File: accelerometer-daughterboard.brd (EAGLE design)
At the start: 17.8 x 25.4 mm, 19 parts, among them U1 LIS3DHTR

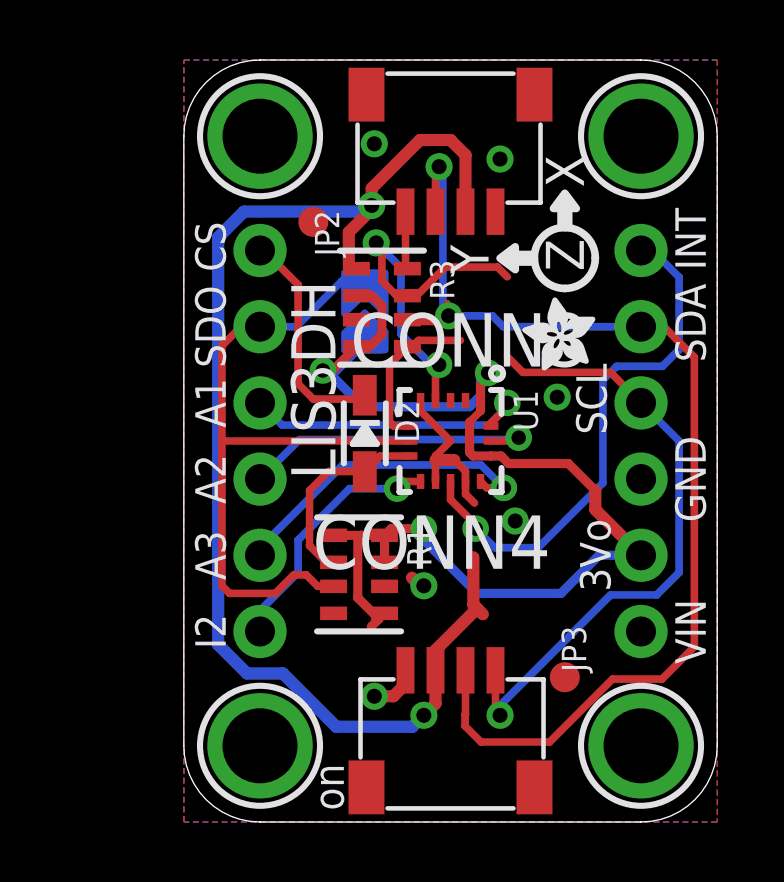
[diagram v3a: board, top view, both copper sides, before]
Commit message: Remove connector headers
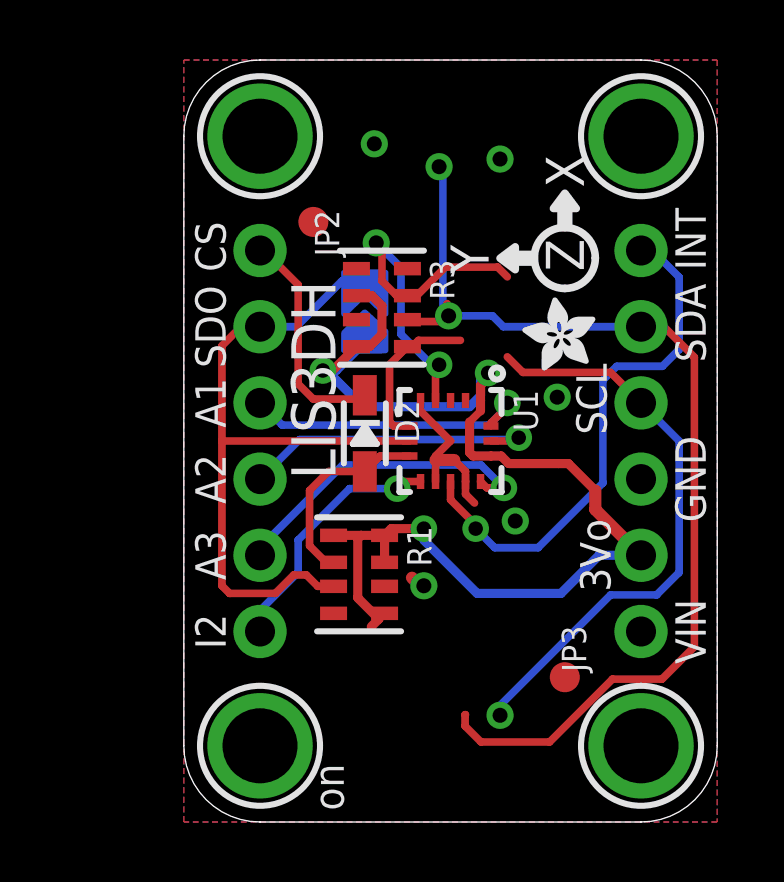
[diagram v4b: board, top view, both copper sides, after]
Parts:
- removed CONN3, CONN4: STEMMA_I2C_QT, microbuilder:JST_SH4
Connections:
- net GND: no longer CONN3.1, CONN4.1
- net SCL: no longer CONN3.4, CONN4.4
- net SDA: no longer CONN3.3, CONN4.3
- net VCC: no longer CONN3.2, CONN4.2
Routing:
- net VCC: track 42.5 -> 0.27 mm, vias 2 -> 0
- net SCL: track 22.8 -> 19.6 mm
- net SDA: track 37.9 -> 35.1 mm
- net GND: track 7.71 -> 6.04 mm, vias 6 -> 5
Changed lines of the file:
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@@
 <attribute name="BOM" value="EXCLUDE" x="2.54" y="22.86" size="1.016" layer="27" font="vector" ratio="14" rot="R90" display="off"/>
-</element>
-<element name="CONN3" library="microbuilder" package="JST_SH4" value="STEMMA_I2C_QT" x="8.89" y="22.86" smashed="yes" rot="R180">
-<attribute name="NAME" x="13.49" y="16.96" size="1.778" layer="25" rot="R180"/>
-</element>
-<element name="CONN4" library="microbuilder" package="JST_SH4" value="STEMMA_I2C_QT" x="8.89" y="2.54" smashed="yes">
-<attribute name="NAME" x="4.29" y="8.44" size="1.778" layer="25"/>
 </element>
 <element name="FID3" library="microbuilder" package="FIDUCIAL_1MM" value="FIDUCIAL_1MM" x="12.7" y="4.826" smashed="yes" rot="R90">
@@
 <signals>
 <signal name="GND" class="1">
-<contactref element="CONN4" pad="1"/>
-<contactref element="CONN3" pad="1"/>
 <polygon width="0.254" layer="1">
 <vertex x="0" y="0"/>
@@
 <vertex x="17.78" y="0"/>
 </polygon>
-<via x="6.35" y="4.191" extent="1-16" drill="0.5"/>
 <via x="10.541" y="22.098" extent="1-16" drill="0.5"/>
-<wire x1="7.39" y1="5.054" x2="7.34" y2="5.004" width="0.4064" layer="1"/>
-<wire x1="7.34" y1="5.004" x2="7.34" y2="4.546" width="0.4064" layer="1"/>
-<wire x1="7.34" y1="4.546" x2="6.985" y2="4.191" width="0.4064" layer="1"/>
-<wire x1="6.985" y1="4.191" x2="6.35" y2="4.191" width="0.4064" layer="1"/>
 <contactref element="U1" pad="5"/>
 <contactref element="U1" pad="10"/>
@@
 <via x="11.049" y="10.033" extent="1-16" drill="0.5"/>
 <via x="12.446" y="14.1605" extent="1-16" drill="0.5"/>
-<wire x1="10.541" y1="22.098" x2="10.39" y2="20.346" width="0" layer="19" extent="1-1"/>
 <wire x1="6.35" y1="22.606" x2="10.541" y2="22.098" width="0" layer="19" extent="1-1"/>
-<wire x1="12.446" y1="14.1605" x2="10.39" y2="20.346" width="0" layer="19" extent="1-1"/>
+<wire x1="12.446" y1="14.1605" x2="10.541" y2="22.098" width="0" layer="19" extent="1-1"/>
 <wire x1="15.24" y1="11.43" x2="12.446" y2="14.1605" width="0" layer="19" extent="1-1"/>
 <wire x1="9.39" y1="11.35" x2="12.446" y2="14.1605" width="0" layer="19" extent="1-1"/>
@@
 <wire x1="7.874" y1="7.874" x2="8.001" y2="7.874" width="0" layer="19" extent="1-1"/>
 <wire x1="6.692" y1="7.855" x2="7.6054" y2="8.1426" width="0" layer="19" extent="1-1"/>
-<wire x1="7.39" y1="5.054" x2="7.874" y2="7.874" width="0" layer="19" extent="1-1"/>
 </signal>
 <signal name="SDA">
-<contactref element="CONN4" pad="3"/>
-<contactref element="CONN3" pad="3"/>
 <wire x1="8.7875" y1="16.872" x2="8.597" y2="16.6815" width="0.254" layer="1"/>
 <wire x1="7.5175" y1="16.6815" x2="8.597" y2="16.6815" width="0.254" layer="1"/>
@@
 <wire x1="8.8265" y1="16.872" x2="8.775" y2="16.9235" width="0.254" layer="1"/>
 <wire x1="8.775" y1="17.283" x2="8.775" y2="16.9235" width="0.254" layer="1"/>
-<wire x1="9.39" y1="5.054" x2="9.39" y2="3.57860625" width="0.254" layer="1"/>
 <wire x1="9.39" y1="3.57860625" x2="9.37539375" y2="3.57860625" width="0.254" layer="1"/>
 <wire x1="9.37539375" y1="3.57860625" x2="9.37539375" y2="3.19760625" width="0.254" layer="1"/>
-<wire x1="8.39" y1="20.346" x2="8.39" y2="21.725" width="0.254" layer="1"/>
 <wire x1="8.39" y1="21.725" x2="8.509" y2="21.844" width="0.254" layer="1"/>
 <via x="8.509" y="21.844" extent="1-16" drill="0.5"/>
@@
 </signal>
 <signal name="SCL">
-<contactref element="CONN4" pad="4"/>
-<contactref element="CONN3" pad="4"/>
-<wire x1="7.39" y1="20.346" x2="7.39" y2="18.509" width="0.254" layer="1"/>
-<wire x1="10.39" y1="5.054" x2="10.39" y2="3.707" width="0.254" layer="1"/>
 <wire x1="10.39" y1="3.707" x2="10.541" y2="3.556" width="0.254" layer="1"/>
 <via x="10.541" y="3.556" extent="1-16" drill="0.5"/>
@@
 <wire x1="15.7607" y1="7.5692" x2="16.51" y2="8.3185" width="0.254" layer="16"/>
 <wire x1="16.51" y1="8.3185" x2="16.51" y2="12.7" width="0.254" layer="16"/>
-<wire x1="10.783" y1="15.506" x2="7.39" y2="18.509" width="0" layer="19" extent="1-1"/>
 </signal>
 <signal name="SCL_3V">
@@
 </signal>
 <signal name="VCC" class="1">
-<contactref element="CONN3" pad="2"/>
-<contactref element="CONN4" pad="2"/>
-<wire x1="9.652" y1="8.824" x2="9.652" y2="7.239" width="0.4064" layer="1"/>
-<wire x1="9.652" y1="7.239" x2="9.7765" y2="7.1145" width="0.4064" layer="1"/>
-<wire x1="9.7765" y1="7.1145" x2="9.967" y2="6.924" width="0.4064" layer="1"/>
-<wire x1="8.39" y1="5.054" x2="8.39" y2="5.728" width="0.4064" layer="1"/>
-<wire x1="8.39" y1="5.728" x2="9.7765" y2="7.1145" width="0.4064" layer="1"/>
-<wire x1="9.39" y1="20.346" x2="9.39" y2="22.233" width="0.4064" layer="1"/>
-<wire x1="9.39" y1="22.233" x2="8.89" y2="22.733" width="0.4064" layer="1"/>
-<wire x1="8.89" y1="22.733" x2="7.874" y2="22.733" width="0.4064" layer="1"/>
-<wire x1="6.262" y1="20.5495" x2="6.262" y2="21.121" width="0.4064" layer="1"/>
-<wire x1="7.874" y1="22.733" x2="6.262" y2="21.121" width="0.4064" layer="1"/>
-<via x="6.262" y="20.5495" extent="1-16" drill="0.5"/>
-<wire x1="6.262" y1="20.5495" x2="6.262" y2="20.4225" width="0.4064" layer="1"/>
-<wire x1="6.262" y1="20.4225" x2="5.5" y2="19.6605" width="0.4064" layer="1"/>
-<wire x1="5.5" y1="19.6605" x2="5.5" y2="18.699" width="0.4064" layer="1"/>
-<wire x1="2.003425" y1="20.3454" x2="6.0579" y2="20.3454" width="0.4064" layer="16"/>
-<wire x1="6.262" y1="20.5495" x2="6.0579" y2="20.3454" width="0.4064" layer="16"/>
-<via x="8.001" y="3.556" extent="1-16" drill="0.5"/>
-<wire x1="8.39" y1="5.054" x2="8.39" y2="3.945" width="0.4064" layer="1"/>
-<wire x1="8.39" y1="3.945" x2="8.001" y2="3.556" width="0.4064" layer="1"/>
 <contactref element="JP3" pad="1"/>
 <wire x1="15.047" y1="6.543" x2="15.24" y2="6.35" width="0.4064" layer="1"/>
-<wire x1="8.001" y1="3.556" x2="7.62" y2="3.175" width="0.4064" layer="16"/>
-<wire x1="2.105025" y1="4.953" x2="1.143" y2="5.915025" width="0.4064" layer="16"/>
-<wire x1="1.143" y1="19.484975" x2="2.003425" y2="20.3454" width="0.4064" layer="16"/>
-<wire x1="7.62" y1="3.175" x2="5.08" y2="3.175" width="0.4064" layer="16"/>
-<wire x1="5.08" y1="3.175" x2="3.302" y2="4.953" width="0.4064" layer="16"/>
-<wire x1="3.302" y1="4.953" x2="2.105025" y2="4.953" width="0.4064" layer="16"/>
-<wire x1="1.143" y1="5.915025" x2="1.143" y2="19.484975" width="0.4064" layer="16"/>
-<wire x1="9.967" y1="6.924" x2="15.047" y2="6.543" width="0" layer="19" extent="1-1"/>
 </signal>
 <signal name="CS">

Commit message: Remove through-holes
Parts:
- removed JP2, JP3: (no value), microbuilder:1X06_ROUND_70
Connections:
- removed net SCL: JP3.4
- removed net SDA: JP3.5
- removed net VCC: JP3.1
- net 3.3V: no longer JP3.2
- net ADC1: no longer JP2.3
- net ADC2: no longer JP2.4
- net ADC3: no longer JP2.5
- net CS: no longer JP2.1
- net GND: no longer JP3.3
- net INT1: no longer JP3.6
- net INT2: no longer JP2.6
- net SDO: no longer JP2.2
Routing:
- net SDA: track 35.1 -> 0.00 mm, vias 2 -> 0
- net SCL: track 19.6 -> 0.00 mm, vias 1 -> 0
- net 3.3V: track 40.1 -> 36.5 mm
- net ADC2: track 10.2 -> 8.30 mm
- net SDO: track 24.2 -> 22.3 mm
- net ADC1: track 9.92 -> 8.88 mm
- net INT2: track 8.46 -> 7.76 mm

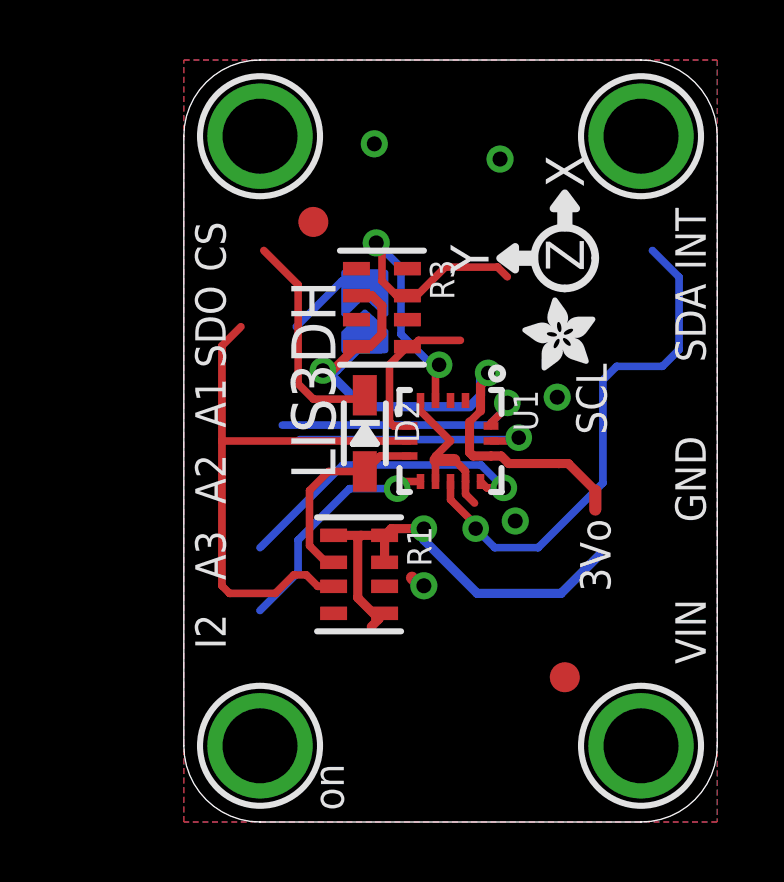
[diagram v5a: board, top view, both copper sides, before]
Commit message: Hardwire CS to I2C mode; add pads; remove un-used board elements
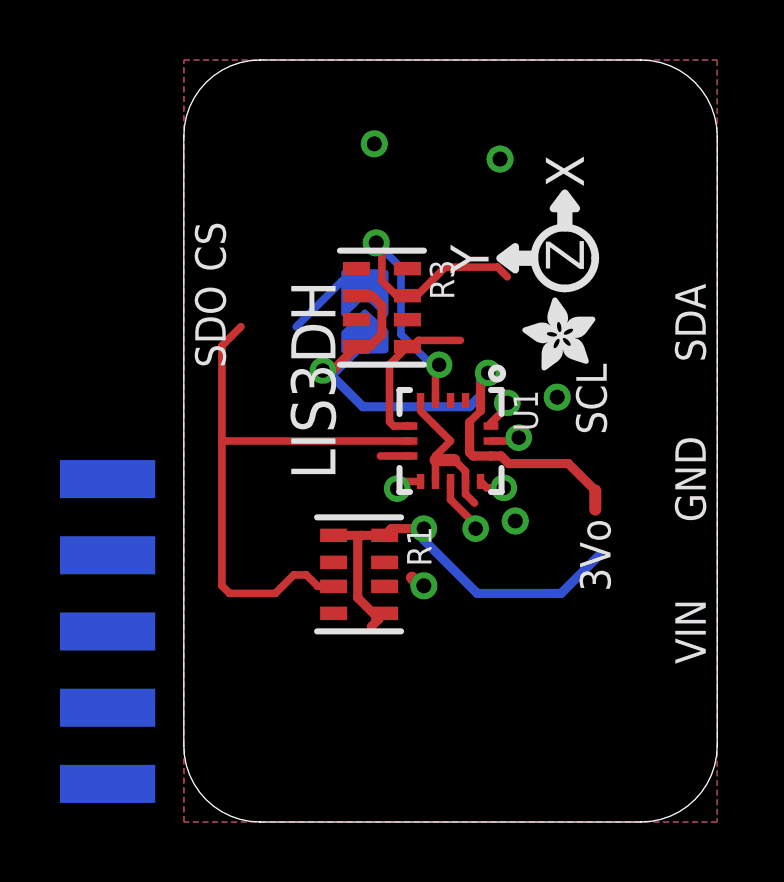
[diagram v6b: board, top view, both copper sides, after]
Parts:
- removed D2: 1N4148, microbuilder:SOD-323
- removed FID3, FID4: FIDUCIAL_1MM, microbuilder:FIDUCIAL_1MM
- removed U$17, U$19, U$21: MOUNTINGHOLE2.5, microbuilder:MOUNTINGHOLE_2.5_PLATED
- removed U$30, U$31: (no value), silks:STEMMAQT
- U$1: value MOUNTINGHOLE2.5 -> ALEX_CONN5; device microbuilder:MOUNTINGHOLE_2.5_PLATED -> TestBoard_2_2_LiPo:ALEX_CONN5
- moved U$1 6.35 mm to (-2.54, 6.35), flipped to the bottom, turned to 0 degrees
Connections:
- removed net CS: D2.C
- removed net N$2: D2.A, R1.2, U1.8
- net 3.3V: now also U1.8; no longer R1.7
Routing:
- net INT1: track 17.4 -> 1.92 mm
- net ADC3: track 10.5 -> 0.87 mm
- net CS: track 7.40 -> 0.00 mm
- net ADC2: track 8.30 -> 1.06 mm
- net ADC1: track 8.88 -> 1.99 mm
- net INT2: track 7.76 -> 0.88 mm
- net N$2: track 6.70 -> 0.00 mm
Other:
- board text removed: "A1"
- board text removed: "A2"
- board text removed: "A3"
- board text removed: "I2"
- board text removed: "INT"
- board text removed: "VLogic/Vcc: 3-5VDC"
- board text removed: "on"

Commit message: USe 0603 resistors
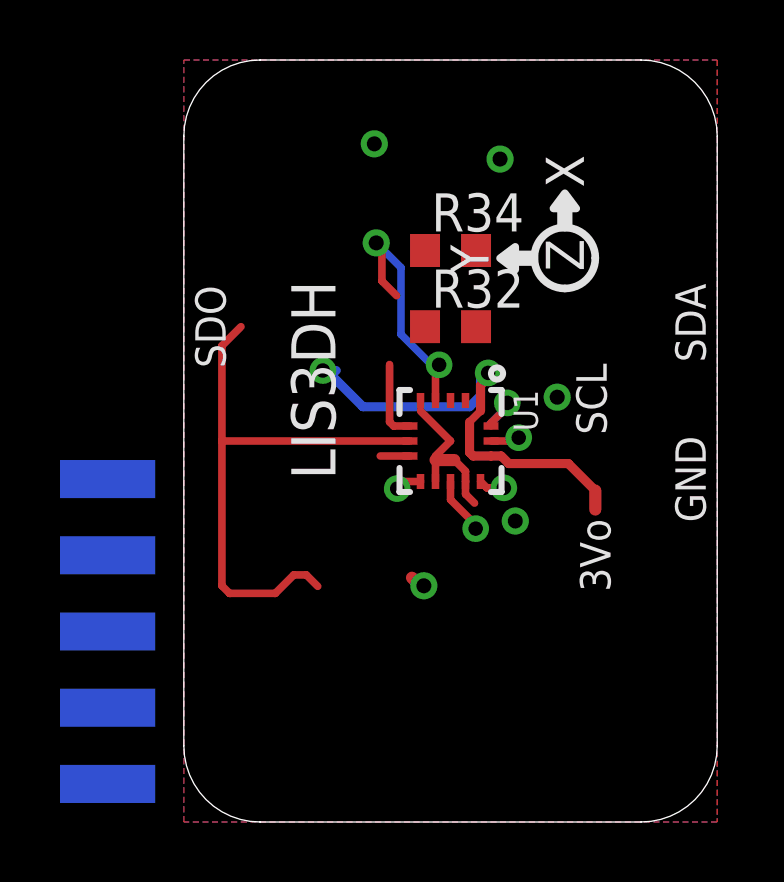
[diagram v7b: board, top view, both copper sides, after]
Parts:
- removed R1, R3: 10K, microbuilder:RESPACK_4X0603
- removed SJ1: (no value), microbuilder:SOLDERJUMPER_ARROW_NOPASTE
- removed U$12: (no value), microbuilder:ADAFRUIT_2.5MM
- added R32, R34: 10K, rcl:R0603
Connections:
- net 3.3V: now also R32.2, R34.2; no longer R1.1, R1.8, R3.2, R3.4, SJ1.1
- net GND: no longer R1.6
- net SCL_3V: now also R32.1; no longer R3.7
- net SDA_3V: now also R34.1; no longer R3.5
- net SDO: no longer R1.3, SJ1.2
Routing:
- net 3.3V: track 36.6 -> 16.9 mm, vias 3 -> 2
- net SCL_3V: track 12.6 -> 8.36 mm
- net SDO: track 22.3 -> 18.9 mm
- net SDA_3V: track 5.35 -> 2.65 mm
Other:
- board text removed: "CS"
- board text removed: "VIN"

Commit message: Add vias; remove some wires
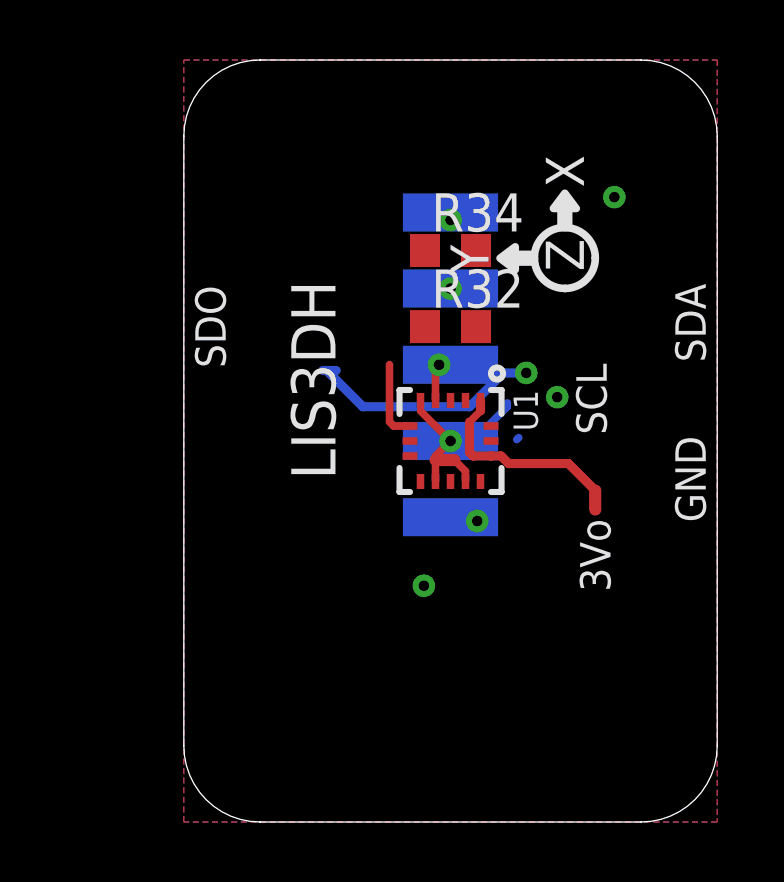
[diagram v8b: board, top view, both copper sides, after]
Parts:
- moved U$1 14.5 mm to (8.89, 15.2)
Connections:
- net 3.3V: now also U$1.P$5
- net GND: now also U$1.P$1
- net SCL_3V: now also U$1.P$3
- net SDA_3V: now also U$1.P$2
- net SDO: now also U$1.P$4
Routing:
- net SDO: track 18.9 -> 0.00 mm, vias 0 -> 1
- net SCL_3V: track 8.36 -> 1.49 mm, vias 2 -> 1
- net INT1: track 1.92 -> 0.00 mm, vias 1 -> 0
- net 3.3V: track 16.9 -> 15.3 mm, vias 2 -> 1
- net GND: track 6.04 -> 4.82 mm
- net ADC1: track 1.99 -> 0.99 mm, vias 1 -> 0
- net ADC2: track 1.06 -> 0.09 mm, vias 1 -> 0
- net INT2: track 0.88 -> 0.00 mm, vias 1 -> 0
- net ADC3: track 0.87 -> 0.00 mm, vias 1 -> 0
- net SDA_3V: vias 0 -> 1
